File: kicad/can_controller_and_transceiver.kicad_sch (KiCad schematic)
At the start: 13 parts, among them U20 MCP2515T-I/ML, U22 TCAN337DR, Y1 ASTX-H11-16.000MHZ-I25-T

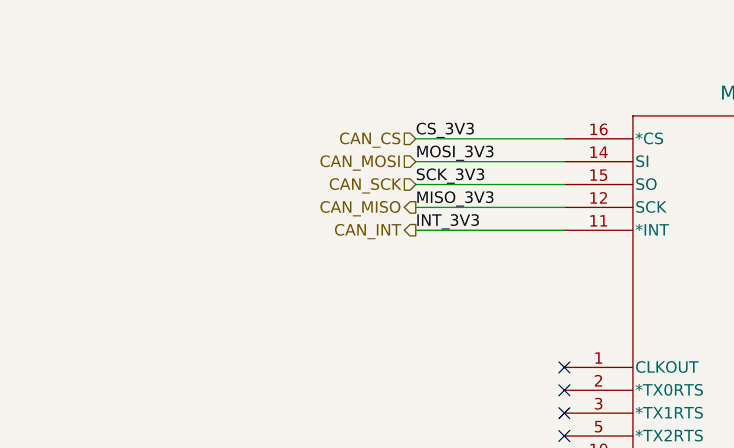
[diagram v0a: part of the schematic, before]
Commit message: add can controller and transceiver, replace platform power connector with one with more appropriate current rating, add return vias
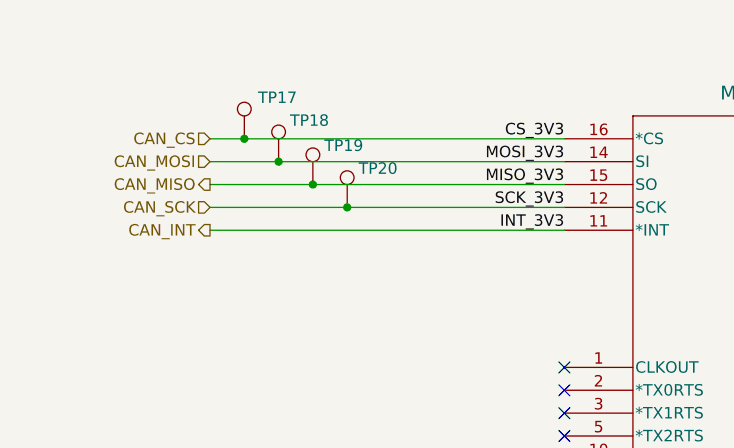
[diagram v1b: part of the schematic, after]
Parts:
- added TP17, TP18, TP19, TP20: TestPoint, TestPoint:TestPoint_Pad_1.0x1.0mm, symbol Connector:TestPoint
- R34, R35, R36, R37: footprint Capacitor_SMD:C_0402_1005Metric -> Resistor_SMD:R_0402_1005Metric
- R38: footprint Capacitor_SMD:C_0603_1608Metric -> Resistor_SMD:R_0603_1608Metric
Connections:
- net CAN_CS: now also TP17.1
- net CAN_MISO: now also U20.15 (SO), TP19.1; no longer U20.12 (SCK)
- net CAN_MOSI: now also TP18.1
- net CAN_SCK: now also U20.12 (SCK), TP20.1; no longer U20.15 (SO)
